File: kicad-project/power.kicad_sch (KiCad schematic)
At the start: 7 parts

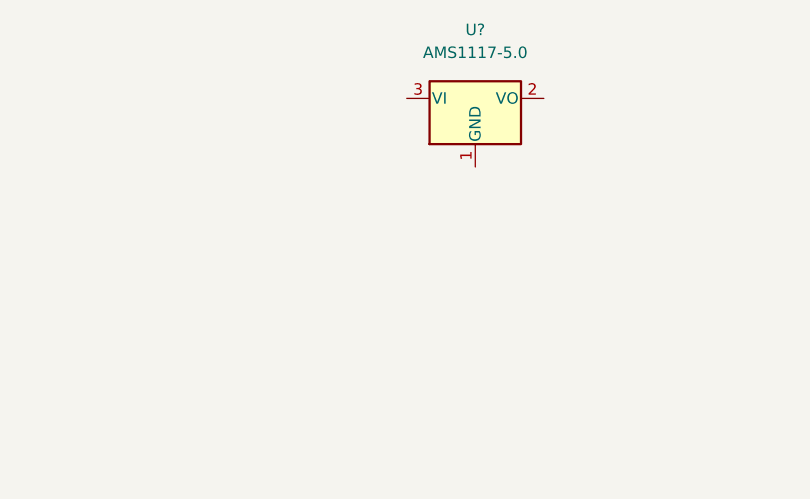
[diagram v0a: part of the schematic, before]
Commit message: hw: rename poject and create project library
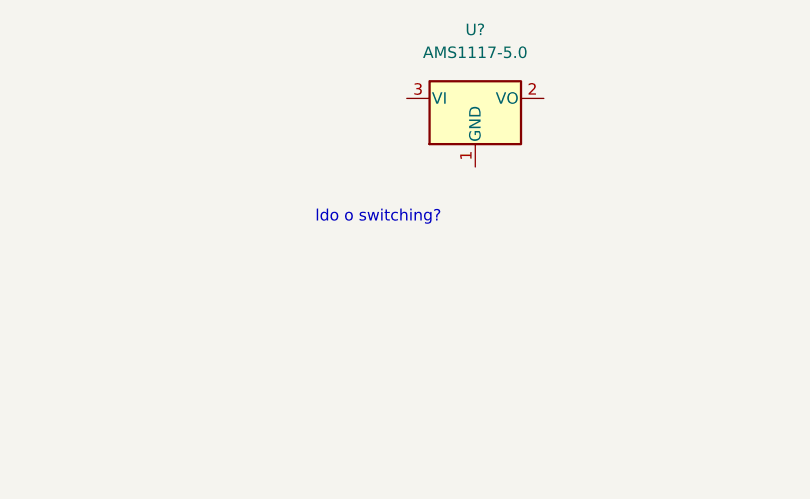
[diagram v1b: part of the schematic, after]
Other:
- note added: "ldo o switching?"
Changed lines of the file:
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@@
 (kicad_sch (version 20211123) (generator eeschema)
   (paper "A4")
+  (text "ldo o switching?\n" (at 172.72 69.85 0)
+    (effects (font (size 1.27 1.27)) (justify left bottom))
+  )
   (symbol (lib_id "Connector:USB_B_Micro") (at 71.12 127 0) (unit 1)
     (in_bom yes) (on_board yes) (fields_autoplaced)

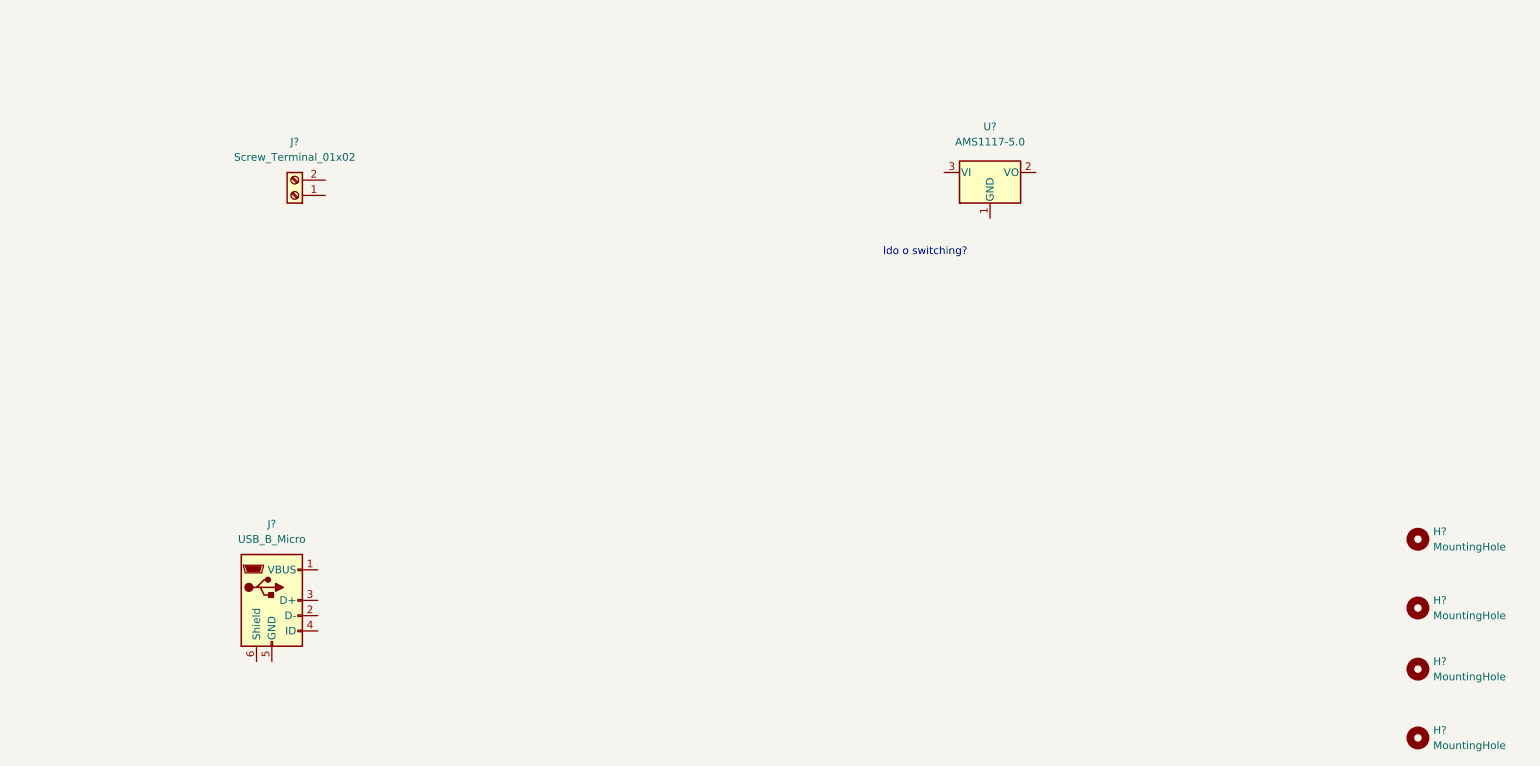
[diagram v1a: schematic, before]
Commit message: hw: add power managment
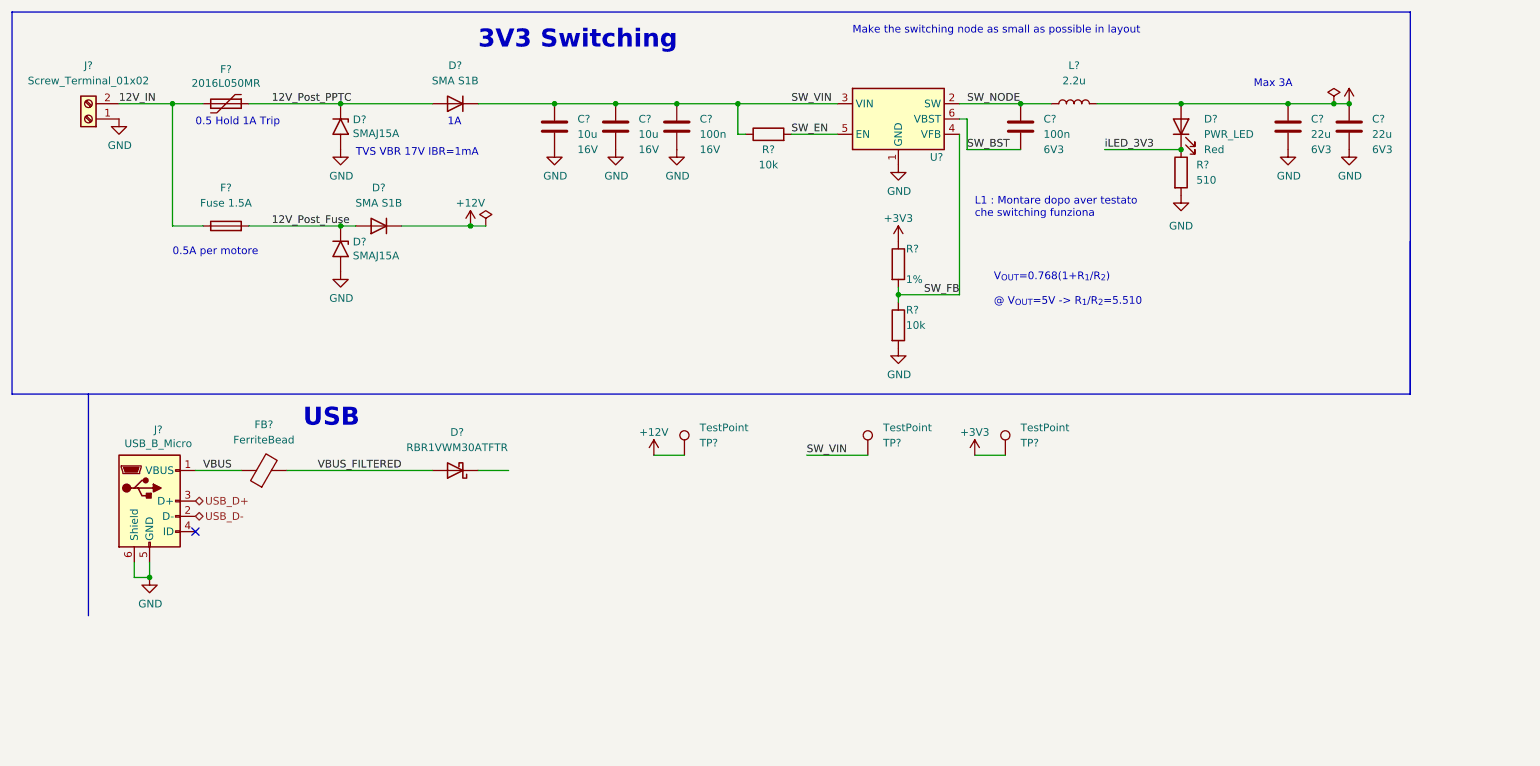
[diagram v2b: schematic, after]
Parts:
- removed H? (x4): MountingHole, symbol Mechanical:MountingHole
- removed J?: USB_B_Micro, symbol Connector:USB_B_Micro
- removed U?: AMS1117-5.0, Package_TO_SOT_SMD:SOT-223-3_TabPin2, symbol Regulator_Linear:AMS1117-5.0
- added C? (x2): 22u, Capacitor_SMD:C_0805_2012Metric, symbol Device:C
- added C? (x2): 10u, Capacitor_SMD:C_0805_2012Metric, symbol Device:C
- added C? (x2): 100n, Capacitor_SMD:C_0603_1608Metric, symbol Device:C
- added D? (x2): SMAJ15A, Diode_SMD:D_SMA, symbol Diode:1.5KExxA
- added D? (x2): SMA S1B, Diode_SMD:D_SMA, symbol Diode:1N4007
- added D?: RBR1VWM30ATFTR, ppse_2021:Package-PMDE, symbol Device:D_Schottky
- added D?: PWR_LED, LED_SMD:LED_0603_1608Metric, symbol Device:LED
- added F?: Fuse 1.5A, ppse_2021:Fuse Holder, symbol Device:Fuse
- added F?: 2016L050MR, ppse_2021:2016L Series PPTC, symbol Device:Polyfuse
- added FB?: FerriteBead, Inductor_SMD:L_0603_1608Metric, symbol Device:FerriteBead
- added J?: USB_B_Micro, Connector_USB:USB_Mini-B_Wuerth_65100516121_Horizontal, symbol Connector:USB_B_Mini
- added L?: 2.2u, ppse_2021:Inductor, symbol Device:L
- added R?: 510, Resistor_SMD:R_0603_1608Metric, symbol Device:R
- added R? (x2): 10k, Resistor_SMD:R_0603_1608Metric, symbol Device:R
- added R?: (no value), Resistor_SMD:R_0603_1608Metric, symbol Device:R
- added TP? (x3): TestPoint, TestPoint:TestPoint_Keystone_5005-5009_Compact, symbol Connector:TestPoint
- added U?: (no value), Package_TO_SOT_SMD:SOT-23-6, symbol Regulator_Switching:TPS563200
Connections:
- net GND: now reaches J?.1 (Pin_1)
- net GND: now also C?.2, C?.2, C?.2, C?.2, C?.2, D?.2 (A2), D?.2 (A2), J?.5 (GND), J?.6 (Shield), R?.2, R?.2, U?.1 (GND)
- net 12V_IN: now reaches J?.2 (Pin_2)
- net 12V_IN: now also F?.1, F?.2
- new net +12V: D?.1 (K), TP?.1
- new net +3V3: R?.1, TP?.1
- new net +5V: C?.1, C?.1, D?.2 (A), L?.2
- new net 12V_Post_Fuse: D?.1 (A1), D?.2 (A), F?.2
- new net 12V_Post_PPTC: D?.1 (A1), D?.2 (A), F?.1
- new net SW_BST: C?.2, U?.6 (VBST)
- new net SW_EN: R?.2, U?.5 (EN)
- new net SW_FB: R?.1, R?.2, U?.4 (VFB)
- new net SW_NODE: C?.1, L?.1, U?.2 (SW)
- new net SW_VIN: C?.1, C?.1, C?.1, D?.1 (K), R?.1, TP?.1, U?.3 (VIN)
- new net USB_D+: J?.3 (D+)
- new net USB_D-: J?.2 (D-)
- new net VBUS: FB?.1, J?.1 (VBUS)
- new net VBUS_FILTERED: D?.2 (A), FB?.2
- new net iLED_3V3: D?.1 (K), R?.1
- no-connect marks 0 -> 1
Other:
- note added: "0.5 Hold 1A Trip"
- note added: "0.5A per motore"
- note added: "1A"
- note added: "3V3 Switching"
- note added: "L1 : Montare dopo aver testato che switching funziona"
- note added: "Make the switching node as small as possible in layout"
- note added: "Max 3A"
- note added: "TVS VBR 17V IBR=1mA"
- note added: "USB"
- note added: "V_{OUT}=0.768(1+R_{1}/R_{2}) @ V_{OUT}=5V -> R_{1}/R_{2}=5.510"
- note removed: "ldo o switching?"
- moved on the sheet: J?

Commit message: hw: update
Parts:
- F?: value Fuse 1.5A -> (none)
- R?: value (none) -> 56k
- U?: value (none) -> TPS563201
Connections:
- net +3V3 is gone; now on net +5V: R?.1, TP?.1
- net SW_VIN: now also D?.1 (K)
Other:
- note added: "DA DIMENSIONARE TUTTI I COMPONENTI !"
- moved on the sheet: TP?

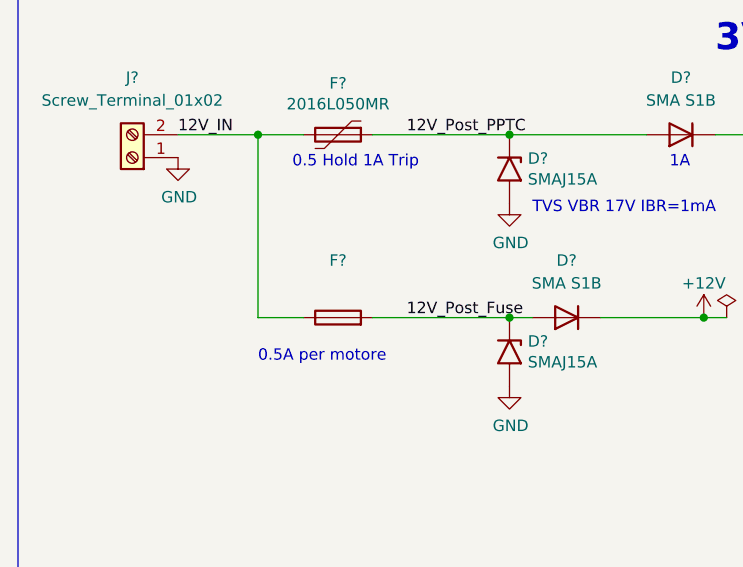
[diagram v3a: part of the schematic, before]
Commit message: hw: add esp8266
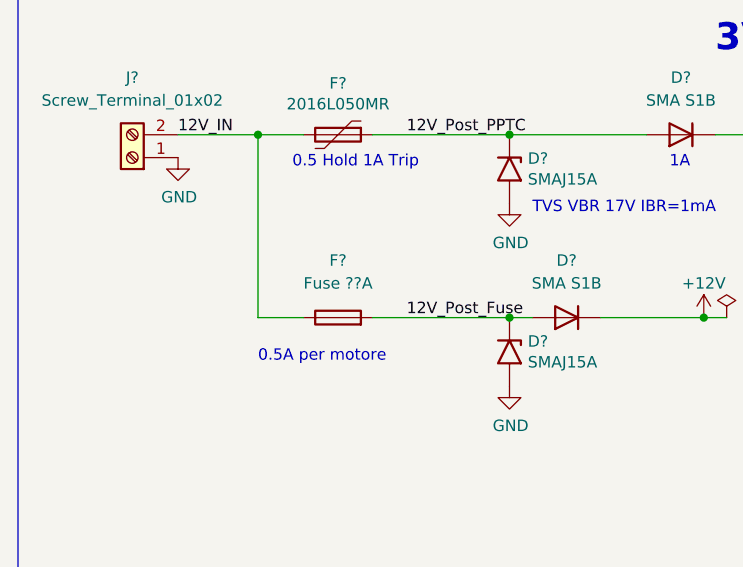
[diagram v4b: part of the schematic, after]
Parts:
- F?: value (none) -> Fuse ??A
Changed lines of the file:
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@@
     (in_bom yes) (on_board yes) (fields_autoplaced)
     (property "Reference" "F?" (id 0) (at 63.5 58.42 90))
-    (property "Value" "" (id 1) (at 63.5 60.96 90))
+    (property "Value" "Fuse ??A" (id 1) (at 63.5 60.96 90))
     (property "Footprint" "ppse_2021:Fuse Holder" (id 2) (at 63.5 66.548 90)
       (effects (font (size 1.27 1.27)) hide)

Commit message: hw: change power management and drivers
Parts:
- removed J?: USB_B_Micro, Connector_USB:USB_Mini-B_Wuerth_65100516121_Horizontal, symbol Connector:USB_B_Mini
- added C? (x4): 10u, Capacitor_SMD:C_0805_2012Metric, symbol Device:C
- added J?: (no value), symbol Connector:USB_C_Receptacle_USB2.0
- added R? (x3): (no value), symbol Device:R
- added U?: (no value), symbol Regulator_Linear:AMS1117-3.3
- added U?: (no value), symbol Regulator_Linear:AMS1117-5.0
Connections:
- net +5V: now also C?.1, U?.2 (VO); no longer C?.1, C?.1, D?.2 (A), L?.2
- net GND: now also C?.2, C?.2, C?.2, C?.2, J?.A1 (GND), J?.A12 (GND), J?.B1 (GND), J?.B12 (GND), R?.2, R?.2, R?.2, U?.1 (GND), U?.1 (GND)
- net SW_VIN: no longer C?.1, C?.1, C?.1, D?.1 (K), D?.1 (K)
- net USB_D+: now also J?.A7 (D-), J?.B7 (D-)
- net USB_D-: now also J?.A6 (D+), J?.B6 (D+)
- net VBUS: now also J?.A4 (VBUS), J?.A9 (VBUS), J?.B4 (VBUS), J?.B9 (VBUS)
- new net: C?.1, C?.1, C?.1, C?.1, C?.1, D?.1 (K), D?.1 (K), U?.3 (VI), U?.3 (VI)
- new net: J?.A5 (CC1), R?.1
- new net: J?.B5 (CC2), R?.1
- new net: J?.S1 (SHIELD), R?.1
- new net: C?.1, C?.1, D?.2 (A), L?.2
- new net +3V3: C?.1, U?.2 (VO)
- no-connect marks 1 -> 3
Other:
- note added: "I out max 1.4A"
- note added: "aggiungo r 0 per sezionare il circuito ?? ams in cascata o parallelo ?"
- note added: "servono ancora qui questi ? oppure bastano in parte all'usb?"
- moved on the sheet: C?, D?, L?, R?, TP?, U?

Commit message: Bipolar pins
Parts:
- J?: value (none) -> USB_C_Receptacle_USB2.0
- R? (x2): value (none) -> 5k1
- R?: value (none) -> 1M
- U?: value (none) -> AMS1117-3.3; footprint (none) -> Package_TO_SOT_SMD:SOT-223-3_TabPin2
- U?: value (none) -> AMS1117-5.0; footprint (none) -> Package_TO_SOT_SMD:SOT-223-3_TabPin2
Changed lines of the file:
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@@
     (in_bom yes) (on_board yes) (fields_autoplaced)
     (property "Reference" "U?" (id 0) (at 171.45 60.96 0))
-    (property "Value" "" (id 1) (at 171.45 63.5 0))
-    (property "Footprint" "" (id 2) (at 171.45 63.5 0)
+    (property "Value" "AMS1117-3.3" (id 1) (at 171.45 63.5 0))
+    (property "Footprint" "Package_TO_SOT_SMD:SOT-223-3_TabPin2" (id 2) (at 171.45 63.5 0)
       (effects (font (size 1.27 1.27)) hide)
     )
@@
     (in_bom yes) (on_board yes) (fields_autoplaced)
     (property "Reference" "J?" (id 0) (at 42.545 97.79 0))
-    (property "Value" "" (id 1) (at 42.545 100.33 0))
+    (property "Value" "USB_C_Receptacle_USB2.0" (id 1) (at 42.545 100.33 0))
     (property "Footprint" "" (id 2) (at 46.355 120.65 0)
       (effects (font (size 1.27 1.27)) hide)
@@
       (effects (font (size 1.27 1.27)) hide)
     )
-    (property "Value" "" (id 1) (at 68.58 113.0299 90)
+    (property "Value" "GND" (id 1) (at 68.58 113.0299 90)
       (effects (font (size 1.27 1.27)) (justify right))
     )
@@
       (effects (font (size 1.27 1.27)) hide)
     )
-    (property "Value" "" (id 1) (at 198.12 63.5 0))
+    (property "Value" "+3V3" (id 1) (at 198.12 63.5 0))
     (property "Footprint" "" (id 2) (at 198.12 68.58 0)
       (effects (font (size 1.27 1.27)) hide)
@@
       (effects (font (size 1.27 1.27)) hide)
     )
-    (property "Value" "" (id 1) (at 39.37 156.21 0))
+    (property "Value" "GND" (id 1) (at 39.37 156.21 0))
     (property "Footprint" "" (id 2) (at 39.37 151.13 0)
       (effects (font (size 1.27 1.27)) hide)
@@
     (in_bom yes) (on_board yes) (fields_autoplaced)
     (property "Reference" "U?" (id 0) (at 171.45 36.83 0))
-    (property "Value" "" (id 1) (at 171.45 39.37 0))
-    (property "Footprint" "" (id 2) (at 171.45 39.37 0)
+    (property "Value" "AMS1117-5.0" (id 1) (at 171.45 39.37 0))
+    (property "Footprint" "Package_TO_SOT_SMD:SOT-223-3_TabPin2" (id 2) (at 171.45 39.37 0)
       (effects (font (size 1.27 1.27)) hide)
     )
@@
     (in_bom yes) (on_board yes)
     (property "Reference" "R?" (id 0) (at 60.325 108.585 90))
-    (property "Value" "" (id 1) (at 63.5 108.585 90))
+    (property "Value" "5k1" (id 1) (at 63.5 108.585 90))
     (property "Footprint" "" (id 2) (at 61.595 112.268 90)
       (effects (font (size 1.27 1.27)) hide)
@@
       (effects (font (size 1.27 1.27)) (justify left))
     )
-    (property "Value" "" (id 1) (at 36.83 148.5899 0)
+    (property "Value" "1M" (id 1) (at 36.83 148.5899 0)
       (effects (font (size 1.27 1.27)) (justify left))
     )
@@
     (in_bom yes) (on_board yes)
     (property "Reference" "R?" (id 0) (at 60.325 115.57 90))
-    (property "Value" "" (id 1) (at 63.5 115.57 90))
+    (property "Value" "5k1" (id 1) (at 63.5 115.57 90))
     (property "Footprint" "" (id 2) (at 61.595 114.808 90)
       (effects (font (size 1.27 1.27)) hide)
@@
       (effects (font (size 1.27 1.27)) hide)
     )
-    (property "Value" "" (id 1) (at 68.58 110.4899 90)
-      (effects (font (size 1.27 1.27)) (justify right))
-    )
+    (property "Value" "GND" (id 1) (at 68.58 110.4899 90)
+      (effects (font (size 1.27 1.27)) (justify right))
+    )

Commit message: hw: update to complete schematic
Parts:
- removed C? (x2): 10u, Capacitor_SMD:C_0805_2012Metric, symbol Device:C
- removed D?: SMA S1B, Diode_SMD:D_SMA, symbol Diode:1N4007
- removed D?: SMAJ15A, Diode_SMD:D_SMA, symbol Diode:1.5KExxA
- removed U?: AMS1117-5.0, Package_TO_SOT_SMD:SOT-223-3_TabPin2, symbol Regulator_Linear:AMS1117-5.0
- added D2: PTVS11VS1UR, Diode_SMD:D_SMA, symbol Diode:1.5KExxA
- added TP4: TestPoint, TestPoint:TestPoint_Keystone_5005-5009_Compact, symbol Connector:TestPoint
- D1: renamed from D?; value SMAJ15A -> PTVS12VS1UR; footprint Diode_SMD:D_SMA -> (none)
- D4: renamed from D?; value RBR1VWM30ATFTR -> SBA130CS_R1_00001; footprint ppse_2021:Package-PMDE -> (none)
- D5: renamed from D?; Color Red -> Green
- F1: renamed from F?; value 2016L050MR -> 2929L-LF075; footprint ppse_2021:2016L Series PPTC -> (none)
- F2: renamed from F?; value Fuse ??A -> C1T-T6; footprint ppse_2021:Fuse Holder -> (none)
- gave numbers to parts that had none: 25
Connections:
- net 12V_Post_Fuse is gone; now on net +12V: F2.2
- net +12V: now also D2.1 (A1)
- net +3V3: now also D5.2 (A), TP4.1
- net +5V: now also C5.1, C6.1, C7.1, L1.2, U2.3 (VI)
- net GND: now also D2.2 (A2)
- net SW_VIN: now also C1.1, C2.1, C3.1, D3.1 (K), D4.1 (K)
- no-connect marks 3 -> 2
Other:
- note added: "0.75 Hold 1.5A Trip"
- note added: "1.5A"
- note added: "6A"
- note added: "L1 : Montare dopo aver testato che lo switching funzioni"
- note added: "TUTTI I FOORPRINT SONO DA VERIFICARE/AGGIUNGERE"
- note added: "TVS VBR 12.85V IBR=1mA"
- note added: "TVS VBR 14V IBR=1mA"
- note added: "Testpoint"
- note removed: "0.5 Hold 1A Trip"
- note removed: "0.5A per motore"
- note removed: "1A"
- note removed: "DA DIMENSIONARE TUTTI I COMPONENTI !"
- note removed: "I out max 1.4A"
- note removed: "L1 : Montare dopo aver testato che switching funziona"
- note removed: "Max 3A"
- note removed: "TVS VBR 17V IBR=1mA"
- note removed: "aggiungo r 0 per sezionare il circuito ?? ams in cascata o parallelo ?"
- note removed: "servono ancora qui questi ? oppure bastano in parte all'usb?"
- moved on the sheet: C1, C2, C3, C4, C5, C6, C7, C8, D1, D3, D4, D5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
